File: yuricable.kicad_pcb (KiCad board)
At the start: 2 copper layers, 66 x 30.5 mm, 40 parts, among them U1 FlipperZero, U2 FlipperZero, X10 SolderPad, X11 SolderPad, X12 SolderPad, X13 SolderPad, X14 SolderPad, X15 SolderPad, X16 SolderPad, X17 SolderPad, X18 SolderPad, X19 SolderPad, X2 SolderPad, X20 SolderPad, X21 SolderPad, X22 SolderPad, X23 SolderPad, X24 SolderPad, X25 SolderPad, X26 SolderPad, X27 SolderPad, X28 SolderPad, X29 SolderPad, X3 SolderPad, X30 SolderPad, X31 SolderPad, X32 SolderPad, X33 SolderPad, X34 SolderPad, X35 SolderPad, X36 SolderPad, X37 SolderPad, X38 SolderPad, X39 SolderPad, X4 SolderPad, X5 SolderPad, X6 SolderPad, X7 SolderPad, X8 SolderPad, X9 SolderPad

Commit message: cleaned up pcb
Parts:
- removed X10, X11, X12, X13, X15, X16, X17, X19, X21, X22, X24, X25, X28, X29, X30, X31, X35, X36, X37, X39: SolderPad, lomalkin_kicad_footprints:Flipper-SolderPad
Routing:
- net GND: track 96.3 -> 65.8 mm
- net /5V: track 17.8 -> 7.62 mm
- net /3.3V: track 17.8 -> 7.62 mm

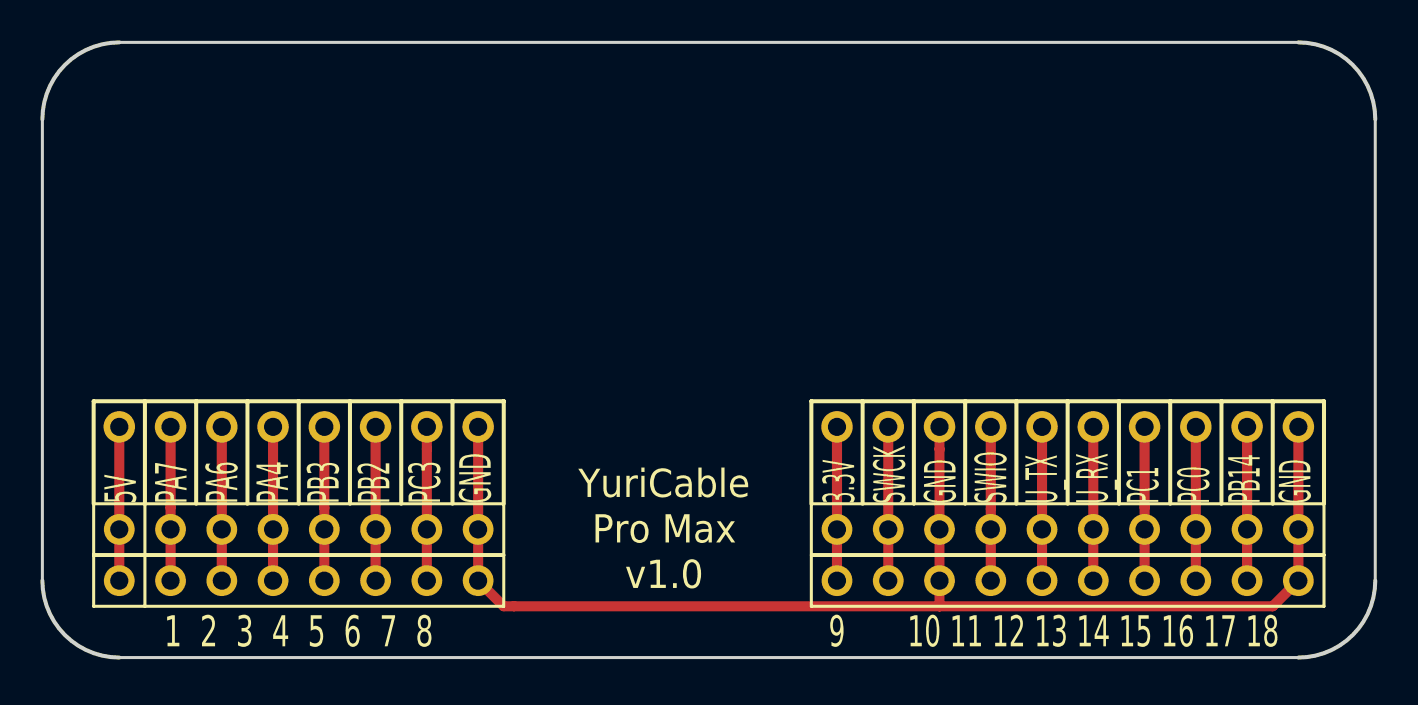
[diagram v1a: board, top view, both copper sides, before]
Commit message: made it smaller and changed the pin labeling
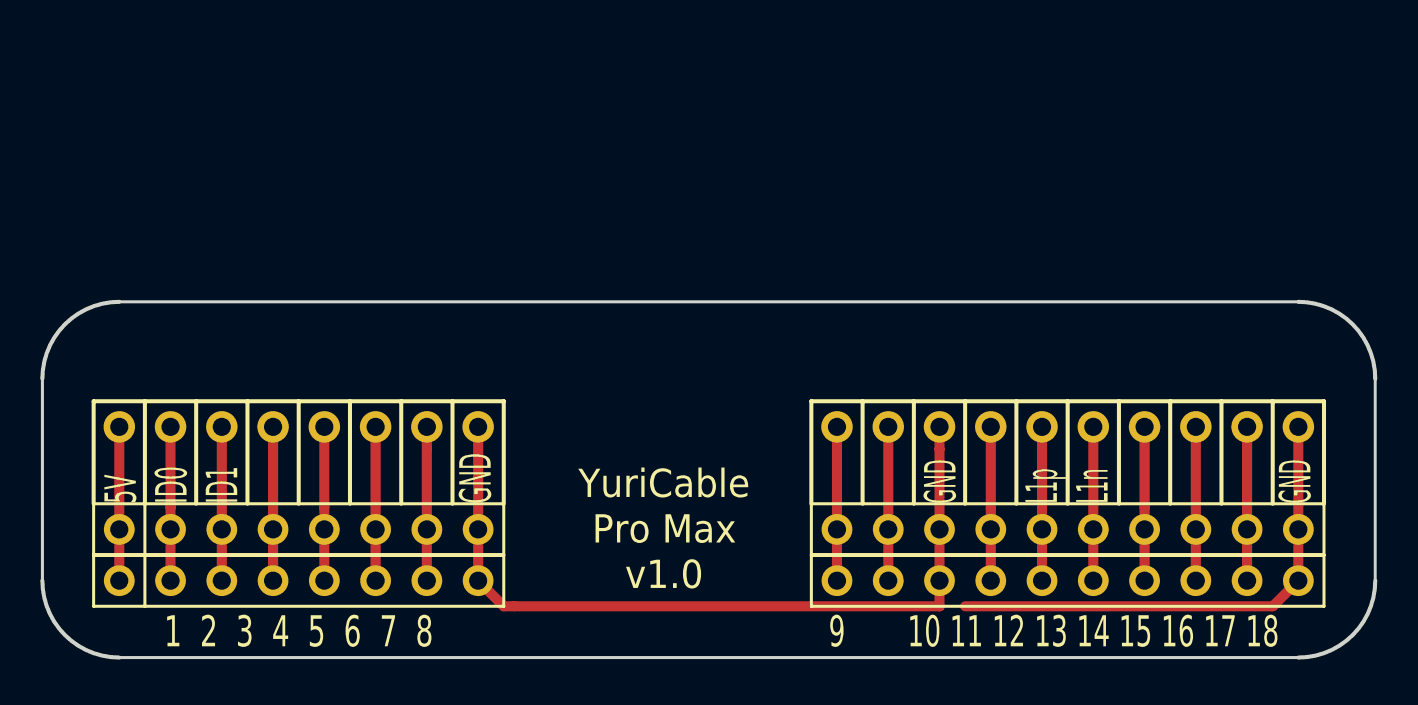
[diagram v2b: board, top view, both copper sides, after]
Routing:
- net GND: track 65.8 -> 64.6 mm
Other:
- board size 66 x 30.5 mm -> 66 x 17.6 mm
- board text added: "5V ID0 ID1 GND"
- board text added: "GND L1p L1n GND"
- board text removed: "3.3V SWCK GND SWIO U_TX U_RX PC1 PC0 PB14 GND"
- board text removed: "5V PA7 PA6 PA4 PB3 PB2 PC3 GND"
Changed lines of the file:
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@@
   (gr_arc (start 125.73 76.2) (mid 124.614077 78.894077) (end 121.92 80.01)
     (stroke (width 0.2) (type solid)) (layer "Edge.Cuts"))
-  (gr_arc (start 121.92 49.53) (mid 124.614077 50.645923) (end 125.73 53.34)
+  (gr_arc (start 121.92 62.384077) (mid 124.614077 63.5) (end 125.73 66.194077)
     (stroke (width 0.2) (type solid)) (layer "Edge.Cuts"))
-  (gr_line (start 125.73 76.2) (end 125.73 53.34)
+  (gr_line (start 125.73 76.2) (end 125.73 66.04)
     (stroke (width 0.15) (type solid)) (layer "Edge.Cuts"))
   (gr_line (start 63.5 80.01) (end 121.92 80.01)
     (stroke (width 0.15) (type solid)) (layer "Edge.Cuts"))
-  (gr_line (start 63.5 49.53) (end 121.92 49.53)
+  (gr_line (start 63.5 62.384077) (end 121.92 62.384077)
     (stroke (width 0.15) (type solid)) (layer "Edge.Cuts"))
-  (gr_line (start 59.69 76.2) (end 59.69 53.34)
+  (gr_line (start 59.69 76.2) (end 59.69 66.04)
     (stroke (width 0.15) (type solid)) (layer "Edge.Cuts"))
-  (gr_arc (start 59.69 53.34) (mid 60.805923 50.645923) (end 63.5 49.53)
+  (gr_arc (start 59.69 66.194077) (mid 60.805923 63.5) (end 63.5 62.384077)
     (stroke (width 0.2) (type solid)) (layer "Edge.Cuts"))
   (gr_text "YuriCable \nPro Max \nv1.0" (at 90.5 73.66) (layer "F.SilkS")
     (effects (font (size 1.4 1.3) (thickness 0.3)))
-  )
-  (gr_text "5V\nPA7\nPA6\nPA4\nPB3\nPB2\nPC3\nGND" (at 72.39 72.39 90) (layer "F.SilkS")
-    (effects (font (size 1.56 0.8) (thickness 0.2)) (justify left))
-  )
-  (gr_text "3.3V\nSWCK\nGND\nSWIO\nU_TX\nU_RX\nPC1\nPC0\nPB14\nGND" (at 110.49 72.39 90) (layer "F.SilkS")
-    (effects (font (size 1.56 0.7) (thickness 0.175)) (justify left))
   )
   (gr_text "10 11 12 13 14 15 16 17 18" (at 111.76 78.74) (layer "F.SilkS")
@@
     (effects (font (size 1.54 1.02) (thickness 0.2)))
   )
+  (gr_text "5V\nID0\nID1\n\n\n\n\nGND" (at 72.39 72.39 90) (layer "F.SilkS")
+    (effects (font (size 1.56 0.8) (thickness 0.2)) (justify left))
+  )
+  (gr_text "\n\nGND\n\nL1p\nL1n\n\n\n\nGND" (at 110.49 72.39 90) (layer "F.SilkS")
+    (effects (font (size 1.56 0.7) (thickness 0.175)) (justify left))
+  )
   (segment (start 63.5 73.66) (end 63.5 76.2) (width 0.5) (layer "F.Cu") (net 1))
   (segment (start 63.5 68.58) (end 63.5 73.66) (width 0.5) (layer "F.Cu") (net 1))
@@
   (segment (start 99.06 68.58) (end 99.06 73.66) (width 0.5) (layer "F.Cu") (net 2))
   (segment (start 104.14 68.58) (end 104.14 69.683086) (width 0.5) (layer "F.Cu") (net 3))
+  (segment (start 105.41 77.47) (end 120.65 77.47) (width 0.5) (layer "F.Cu") (net 3))
   (segment (start 104.14508 77.47) (end 83.058 77.47) (width 0.5) (layer "F.Cu") (net 3))
   (segment (start 120.65 77.47) (end 121.92 76.2) (width 0.5) (layer "F.Cu") (net 3))
@@
   (segment (start 121.92 73.66) (end 121.92 68.58) (width 0.5) (layer "F.Cu") (net 3))
   (segment (start 104.14 77.46492) (end 104.14508 77.47) (width 0.5) (layer "F.Cu") (net 3))
-  (segment (start 104.14508 77.47) (end 120.65 77.47) (width 0.5) (layer "F.Cu") (net 3))
   (segment (start 104.14 69.683086) (end 104.14 73.66) (width 0.5) (layer "F.Cu") (net 3))
   (segment (start 81.28 76.2) (end 82.55 77.47) (width 0.5) (layer "F.Cu") (net 3))

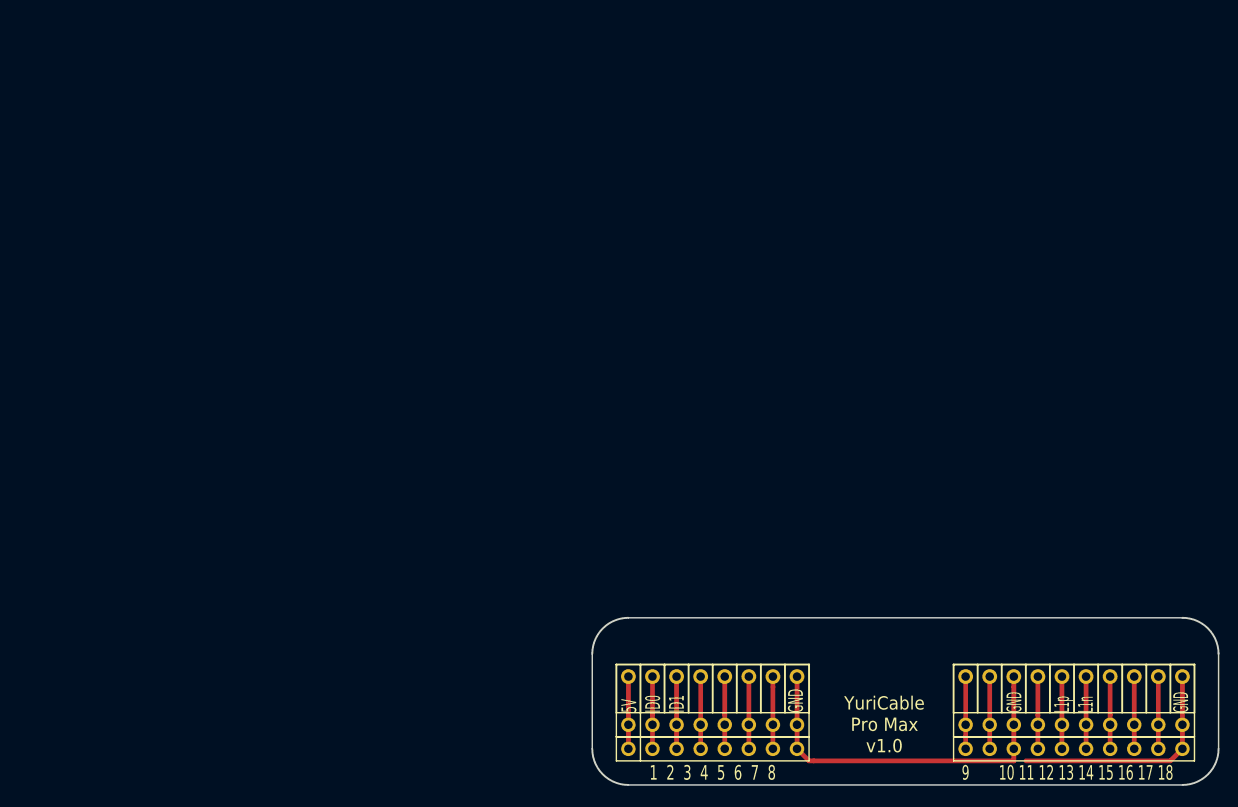
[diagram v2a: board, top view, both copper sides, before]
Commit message: added swd pitch connector and some traces
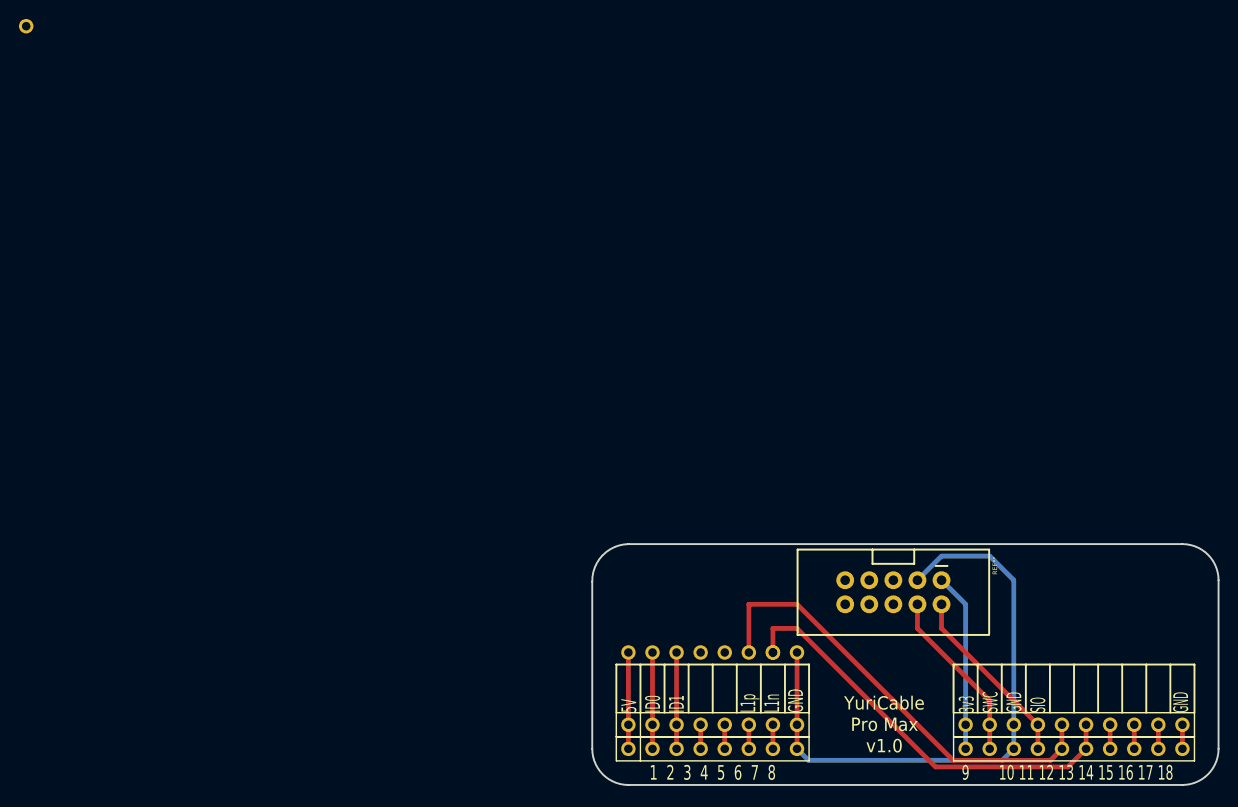
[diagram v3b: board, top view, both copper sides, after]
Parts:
- removed X14, X18, X2, X20, X23, X26, X27, X3, X32, X33, X34, X38, X4, X5, X6, X7, X8, X9: SolderPad, lomalkin_kicad_footprints:Flipper-SolderPad
- added ? (x2): , , F.Cu at (78.7, 66.0)
- added ?: , , F.Cu at (76.2, 66.0)
- added ?: , , F.Cu at (63.5, 66.0)
- added ?: , , F.Cu at (68.6, 66.0)
- added ?: , , F.Cu at (81.3, 66.0)
- added ?: , , F.Cu at (73.7, 66.0)
- added ?: , , F.Cu at (66.0, 66.0)
- added ?: , , F.Cu at (0.00, 0.00)
- added ?: , , F.Cu at (71.1, 66.0)
- added REF**: ARM-JTAG-10-SWD-IDC, ARM-JTAG-SWD:ARM-JTAG-10-SWD-IDC, F.Cu at (91.4, 59.7)
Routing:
- net /UART_RX: track 7.62 -> 44.9 mm
- net /UART_TX: track 7.62 -> 42.9 mm
- net /SWDIO: track 7.62 -> 19.4 mm
- net /3.3V: track 7.62 -> 18.8 mm
- net /SWCLK: track 7.62 -> 18.4 mm
- net /PA7: track 7.62 -> 15.2 mm
- net /SWO: track 7.62 -> 2.54 mm
- net /PC3: track 7.62 -> 2.54 mm
- net /PC1: track 7.62 -> 2.54 mm
- net /PC0: track 7.62 -> 2.54 mm
- net /PB2: track 7.62 -> 2.54 mm
- net /PB14: track 7.62 -> 2.54 mm
- net /PA4: track 7.62 -> 2.54 mm
- net /PA6: track 7.62 -> 10.2 mm
- net /5V: track 7.62 -> 10.2 mm
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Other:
- board size 66 x 17.6 mm -> 66 x 25.4 mm
- board text added: "3v3 SWC GND SIO GND"
- board text added: "5V ID0 ID1 L1p L1n GND"
- board text removed: "5V ID0 ID1 GND"
- board text removed: "GND L1p L1n GND"

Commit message: added some labeling and removed more unneccesary shit
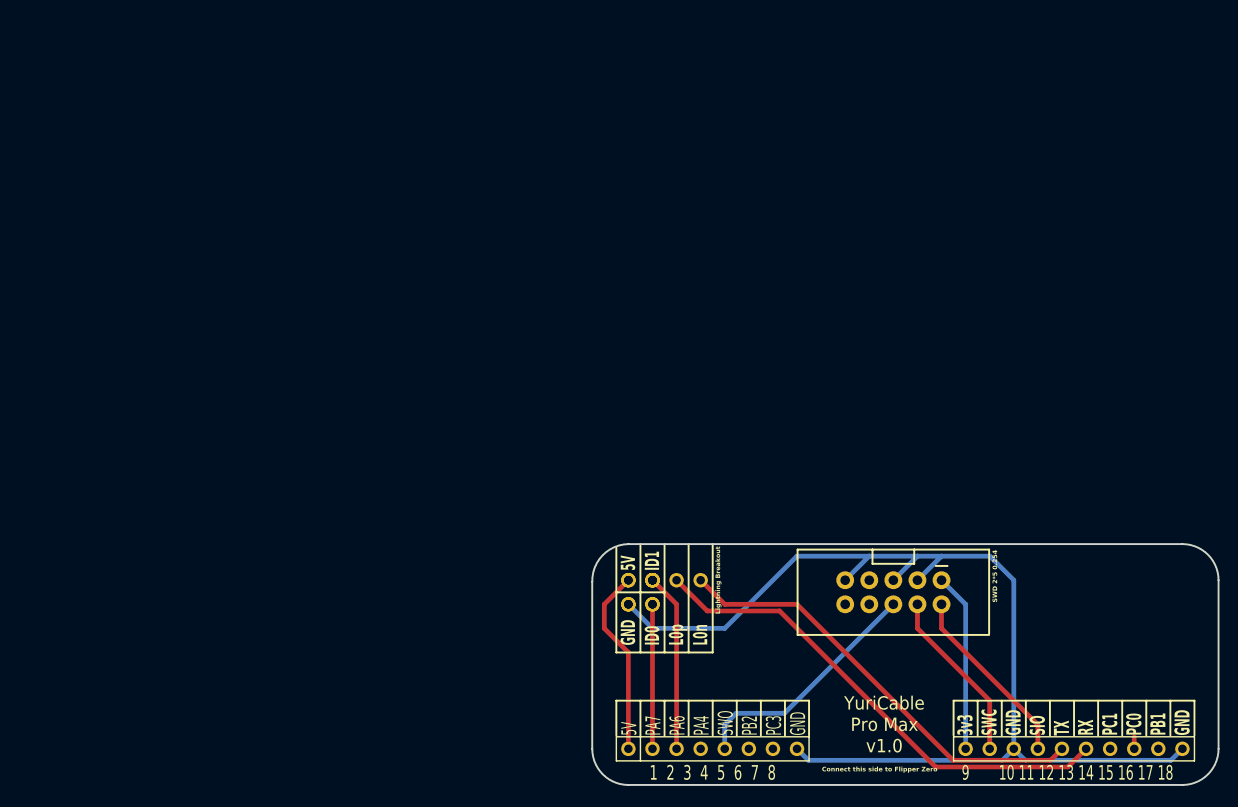
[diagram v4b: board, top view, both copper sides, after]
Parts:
- removed the ? at (78.7, 66.0) (x2)
- removed the ? at (76.2, 66.0)
- removed the ? at (63.5, 66.0)
- removed the ? at (68.6, 66.0)
- removed the ? at (81.3, 66.0)
- removed the ? at (73.7, 66.0)
- removed the ? at (66.0, 66.0)
- removed the ? at (0.00, 0.00)
- removed the ? at (71.1, 66.0)
- removed U2: FlipperZero, lomalkin_kicad_footprints:FlipperZero
- added ? (x2): , , F.Cu at (66.0, 61.0)
- added ? (x4): , , F.Cu at (66.0, 58.4)
- added ? (x2): , , F.Cu at (63.5, 58.4)
- added ?: , , F.Cu at (71.1, 58.4)
- added ? (x2): , , F.Cu at (63.5, 61.0)
- added ?: , , F.Cu at (68.6, 58.4)
- SWD 2*5 0.254: renamed from REF**
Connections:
- SWD 2*5 0.254 pad GND@1: (no net) -> GND
- SWD 2*5 0.254 pad GND@2: (no net) -> GND
- SWD 2*5 0.254 pad GND@3: (no net) -> GND
- SWD 2*5 0.254 pad RESET: (no net) -> RESET
- SWD 2*5 0.254 pad RXI: (no net) -> /RXI
- SWD 2*5 0.254 pad SWCLK: (no net) -> /SWCLK
- SWD 2*5 0.254 pad SWDIO: (no net) -> /SWDIO
- SWD 2*5 0.254 pad SWO: (no net) -> /SWO
- SWD 2*5 0.254 pad TXO: (no net) -> TXO
- SWD 2*5 0.254 pad VREF: (no net) -> VREF
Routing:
- net GND: track 66.6 -> 117.1 mm
- net /SWO: track 2.54 -> 25.6 mm
- net /5V: track 10.2 -> 19.9 mm
- net /PA6: track 10.2 -> 18.8 mm
- net /UART_RX: track 44.9 -> 52.1 mm
- net /UART_TX: track 42.9 -> 46.5 mm
- net /PC3: track 2.54 -> 0.00 mm
- net /PC1: track 2.54 -> 0.00 mm
- net /PB2: track 2.54 -> 0.00 mm
- net /PB14: track 2.54 -> 0.00 mm
- net /PA4: track 2.54 -> 0.00 mm
- net /PC0: track 2.54 -> 1.27 mm
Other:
- board text added: "3v3 SWC GND SIO TX RX PC1 PC0 PB1 GND"
- board text added: "5V"
- board text added: "5V PA7 PA6 PA4 SWO PB2 PC3 GND"
- board text added: "Connect this side to Flipper Zero"
- board text added: "GND"
- board text added: "ID0"
- board text added: "ID1"
- board text added: "L0n"
- board text added: "L0p"
- board text added: "Lightning Breakout"
- board text removed: "3v3 SWC GND SIO GND"
- board text removed: "5V ID0 ID1 L1p L1n GND"

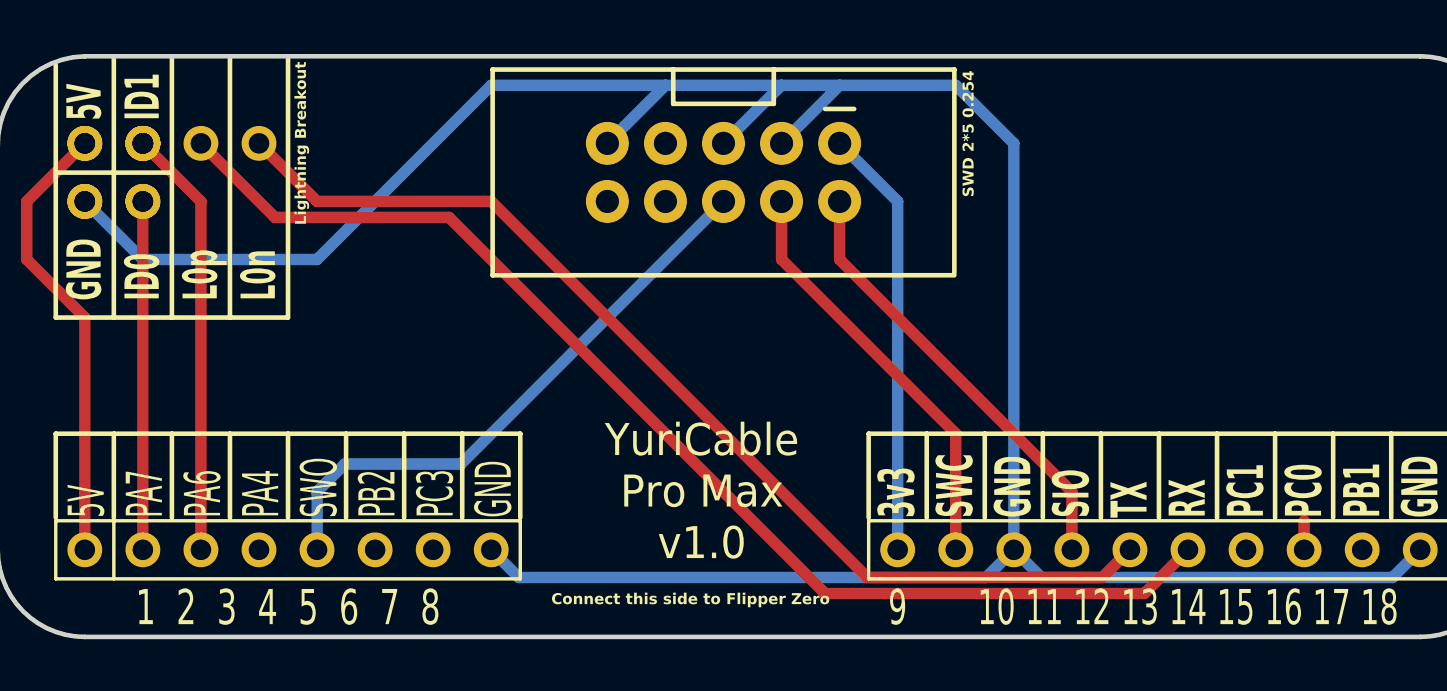
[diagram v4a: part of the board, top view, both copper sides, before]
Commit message: added swd 0.05" footprint and added it ti pcb
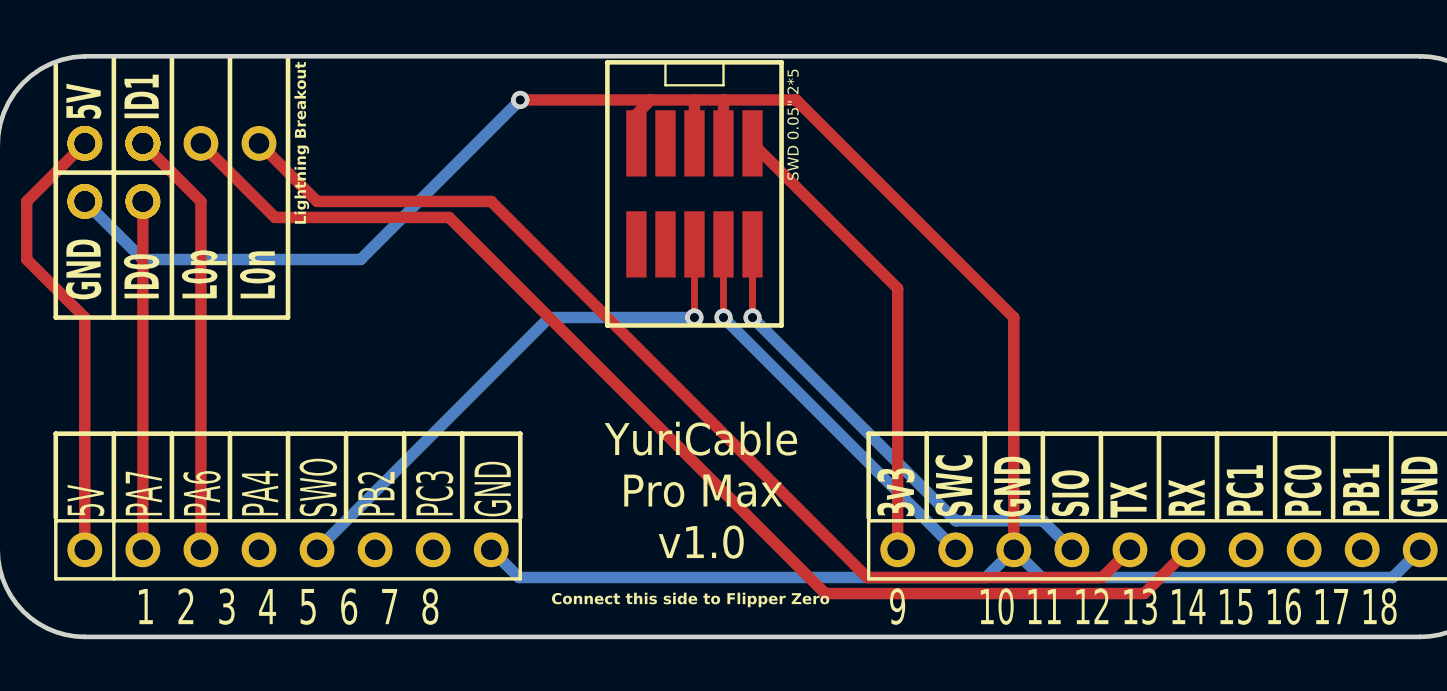
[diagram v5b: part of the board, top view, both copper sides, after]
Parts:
- removed SWD 2*5 0.254: ARM-JTAG-10-SWD-IDC, ARM-JTAG-SWD:ARM-JTAG-10-SWD-IDC
- added SWD 0.05" 2*5: SWD_0.05_2x5, ARM-JTAG-SWD:SWD_0.05_2x5, F.Cu at (90.2, 61.0)
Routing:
- net GND: track 117.1 -> 107.2 mm, vias 0 -> 1
- net /SWDIO: track 19.4 -> 21.4 mm, vias 0 -> 1
- net /SWO: track 25.6 -> 23.9 mm, vias 0 -> 1
- net /3.3V: track 18.8 -> 20.4 mm
- net /PC0: track 1.27 -> 0.00 mm
- net /SWCLK: track 18.4 -> 17.6 mm, vias 0 -> 1
